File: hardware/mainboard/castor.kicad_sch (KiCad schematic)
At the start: 46 parts, among them J7 OSC OUT, Q1 MMBT3906, U10 MCP6001-OT, U7 TL074, U8 TL074, U9 74LVC2G74

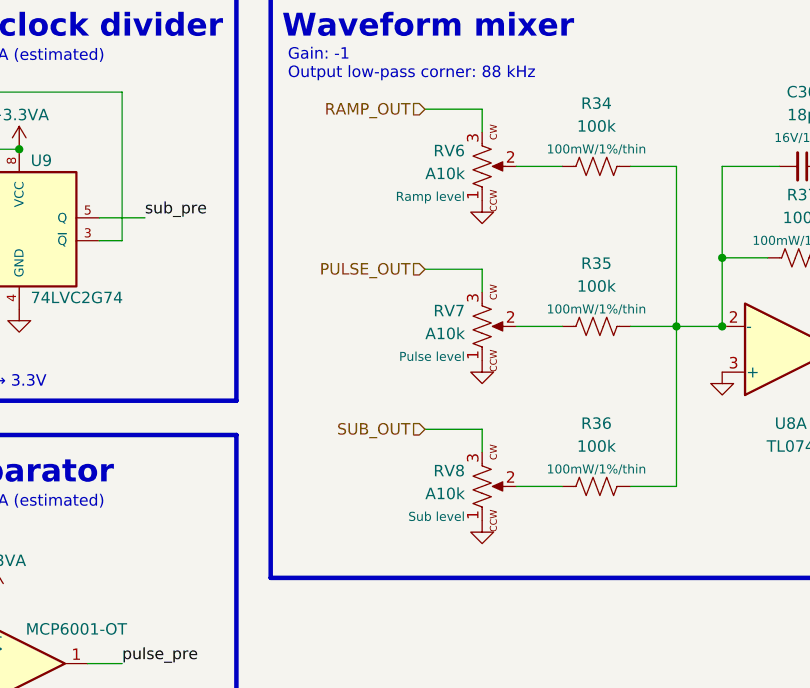
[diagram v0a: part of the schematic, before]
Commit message: hardware: update some labels, fix some fields, re-do fancytext
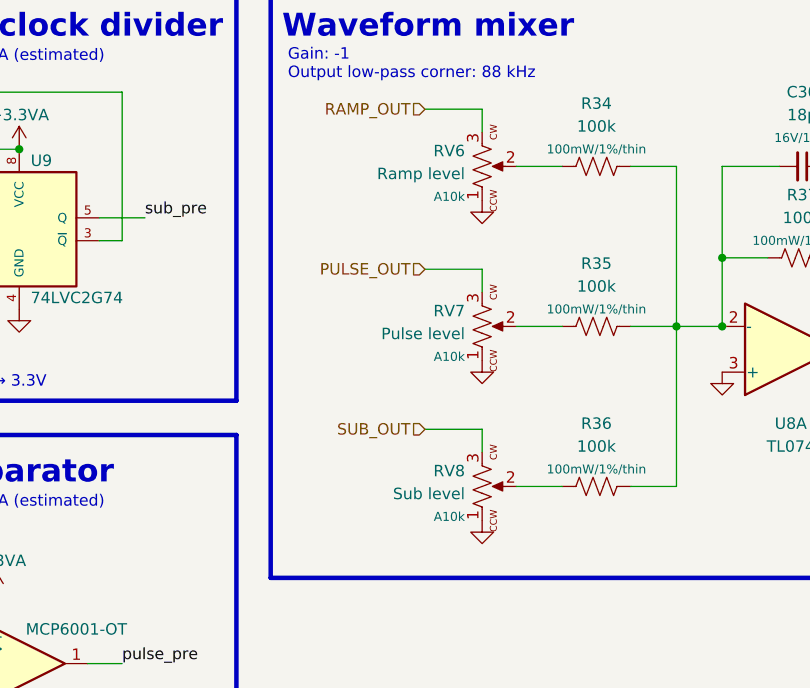
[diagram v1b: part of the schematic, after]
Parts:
- RV6: value A10k -> Ramp level; Rating Ramp level -> A10k
- RV7: value A10k -> Pulse level; Rating Pulse level -> A10k
- RV8: value A10k -> Sub level; Rating Sub level -> A10k
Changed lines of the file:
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@@
       (effects (font (size 1.27 1.27)) (justify left))
     )
-    (property "Value" "A10k" (id 1) (at 90.17 161.4804 90)
+    (property "Value" "Sub level" (id 1) (at 90.17 161.4804 90)
       (effects (font (size 1.27 1.27)) (justify left))
     )
@@
       (effects (font (size 1.27 1.27)) hide)
     )
-    (property "Rating" "Sub level" (id 7) (at 90.17 164.0205 90)
+    (property "Rating" "A10k" (id 7) (at 90.17 164.0205 90)
       (effects (font (size 1 1)) (justify left))
     )
@@
       (effects (font (size 1.27 1.27)) (justify left))
     )
-    (property "Value" "A10k" (id 1) (at 90.17 143.7004 90)
+    (property "Value" "Pulse level" (id 1) (at 90.17 143.7004 90)
       (effects (font (size 1.27 1.27)) (justify left))
     )
@@
       (effects (font (size 1.27 1.27)) hide)
     )
-    (property "Rating" "Pulse level" (id 7) (at 90.17 146.2405 90)
+    (property "Rating" "A10k" (id 7) (at 90.17 146.2405 90)
       (effects (font (size 1 1)) (justify left))
     )
@@
       (effects (font (size 1.27 1.27)) (justify left))
     )
-    (property "Value" "A10k" (id 1) (at 90.17 125.9204 90)
+    (property "Value" "Ramp level" (id 1) (at 90.17 125.9204 90)
       (effects (font (size 1.27 1.27)) (justify left))
     )
@@
       (effects (font (size 1.27 1.27)) hide)
     )
-    (property "Rating" "Ramp level" (id 7) (at 90.17 128.4605 90)
+    (property "Rating" "A10k" (id 7) (at 90.17 128.4605 90)
       (effects (font (size 1 1)) (justify left))
     )

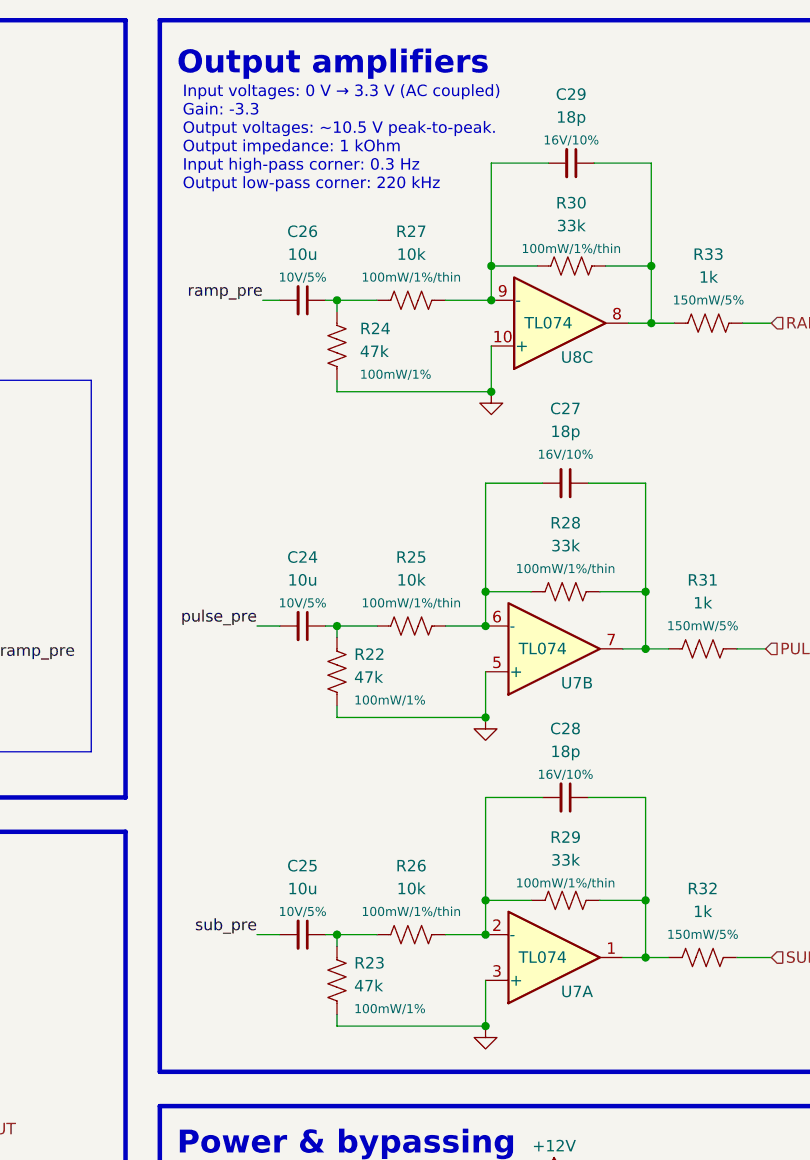
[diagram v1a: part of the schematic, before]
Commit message: hardware: change R22-R24 value to 100k, mark as optional
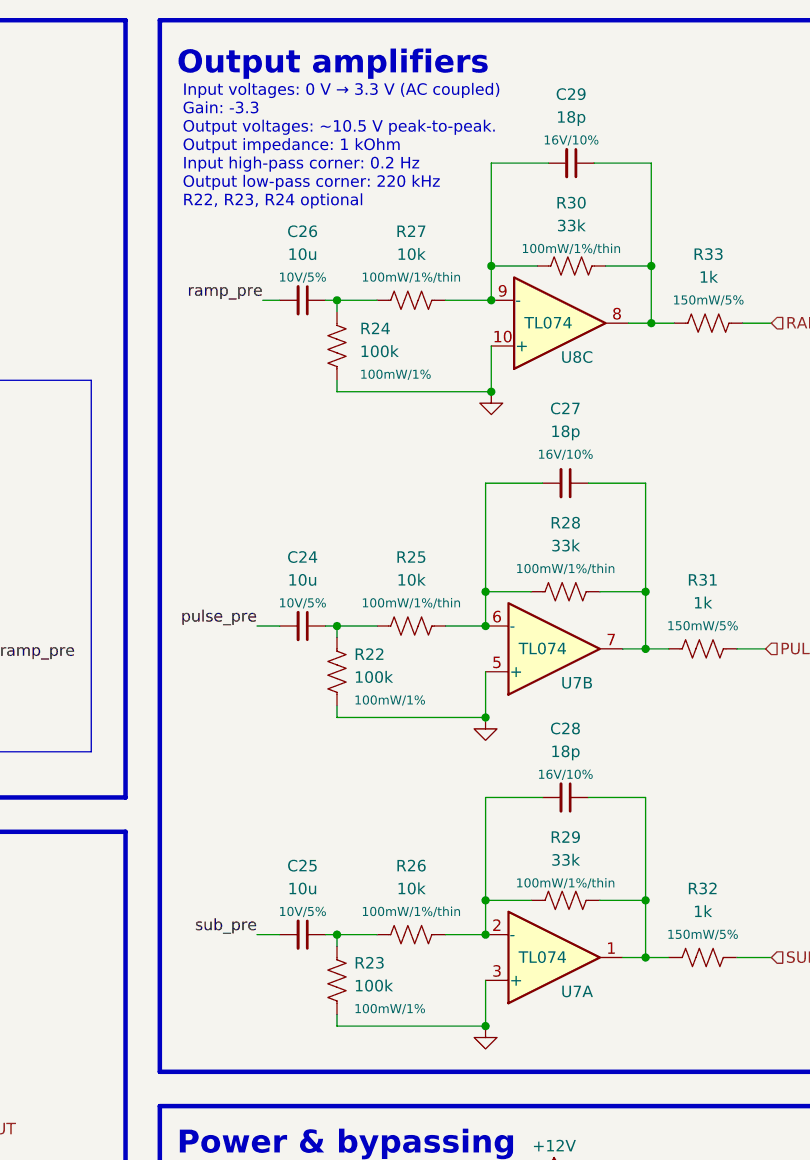
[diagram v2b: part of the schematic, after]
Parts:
- R22, R23, R24: value 47k -> 100k; MPN RC0402FR-0747KL -> RC0402DR-07100KL
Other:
- note added: "Input voltages: 0 V → 3.3 V (AC coupled) Gain: -3.3 Output voltages: ~10.5 V peak-to-peak. Output impedance: 1 kOhm Input high-pass corner: 0.2 Hz Output low-pass corner: 220 kHz R22, R23, R24 optional"
- note removed: "Input voltages: 0 V → 3.3 V (AC coupled) Gain: -3.3 Output voltages: ~10.5 V peak-to-peak. Output impedance: 1 kOhm Input high-pass corner: 0.3 Hz Output low-pass corner: 220 kHz"
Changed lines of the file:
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@@
     (effects (font (size 1.27 1.27) (thickness 0.254) bold) (justify left bottom))
   )
-  (text "Input voltages: 0 V → 3.3 V (AC coupled)\nGain: -3.3\nOutput voltages: ~10.5 V peak-to-peak.\nOutput impedance: 1 kOhm\nInput high-pass corner: 0.3 Hz\nOutput low-pass corner: 220 kHz"
-    (at 181.61 34.29 0)
+  (text "Input voltages: 0 V → 3.3 V (AC coupled)\nGain: -3.3\nOutput voltages: ~10.5 V peak-to-peak.\nOutput impedance: 1 kOhm\nInput high-pass corner: 0.2 Hz\nOutput low-pass corner: 220 kHz\nR22, R23, R24 optional"
+    (at 181.61 36.195 0)
     (effects (font (size 1.27 1.27)) (justify left bottom))
   )
@@
       (effects (font (size 1.27 1.27)) (justify left))
     )
-    (property "Value" "47k" (id 1) (at 201.295 52.0699 0)
+    (property "Value" "100k" (id 1) (at 201.295 52.0699 0)
       (effects (font (size 1.27 1.27)) (justify left))
     )
@@
       (effects (font (size 1.27 1.27)) hide)
     )
-    (property "MPN" "RC0402FR-0747KL" (id 5) (at 198.755 51.435 0)
+    (property "MPN" "RC0402DR-07100KL" (id 5) (at 198.755 51.435 0)
       (effects (font (size 1.27 1.27)) hide)
     )
@@
       (effects (font (size 1.27 1.27)) (justify left))
     )
-    (property "Value" "47k" (id 1) (at 200.66 88.2649 0)
+    (property "Value" "100k" (id 1) (at 200.66 88.2649 0)
       (effects (font (size 1.27 1.27)) (justify left))
     )
@@
       (effects (font (size 1.27 1.27)) hide)
     )
-    (property "MPN" "RC0402FR-0747KL" (id 5) (at 198.755 87.63 0)
+    (property "MPN" "RC0402DR-07100KL" (id 5) (at 198.755 87.63 0)
       (effects (font (size 1.27 1.27)) hide)
     )
@@
       (effects (font (size 1.27 1.27)) (justify left))
     )
-    (property "Value" "47k" (id 1) (at 200.66 122.5549 0)
+    (property "Value" "100k" (id 1) (at 200.66 122.5549 0)
       (effects (font (size 1.27 1.27)) (justify left))
     )
@@
       (effects (font (size 1.27 1.27)) hide)
     )
-    (property "MPN" "RC0402FR-0747KL" (id 5) (at 198.755 121.92 0)
-      (effects (font (size 1.27 1.27)) hide)
-    )
+    (property "MPN" "RC0402DR-07100KL" (id 5) (at 198.755 121.92 0)
+      (effects (font (size 1.27 1.27)) hide)
+    )
